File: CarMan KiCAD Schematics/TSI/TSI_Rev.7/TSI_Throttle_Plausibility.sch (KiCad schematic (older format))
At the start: 67 parts, among them Q2 MMBF170, SW1 TS5A3159DBVT, U16 TS372CDT, U18 MCP6004, U23 DAC5574IDGS, U3 TS912, U30 TLP293, U6 TS912, U7 MCP6004, U8 74ACT11030

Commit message: TSI Should be final schematic
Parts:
- removed U18, U7: MCP6004, TSI_Rev_2021_Footprint_Lib:SOIC127P600X175-14N, symbol TSI_Rev.5-rescue:MCP6004-Amplifier_Operational
- added R126: 5.1K, symbol Device:R
- added R127: 10K, symbol Device:R
- added U18, U7: TLV2464CDR, CarMan General Footprints:SOIC127P600X175-14N, symbol CarMan_KiCAD_Library:TLV2464CDR
- C10, C11, C15, C16, C22, C25, C26, C27, C3, C7, C8: footprint Capacitor_SMD:C_0805_2012Metric_Pad1.15x1.40mm_HandSolder -> Capacitor_SMD:C_0805_2012Metric_Pad1.18x1.45mm_HandSolder
- D2: footprint Package_SO:SO-8_5.3x6.2mm_P1.27mm -> Package_SO:MSOP-8_3x3mm_P0.65mm
- R1, R103, R124, R125, R17, R18, R19, R20, R21, R22, R23, R24, R26, R27, R28, R29, R30, R31, R32, R34, R35, R36, R37, R38, R39, R40, R42, R43, R44, R48, R49, R5, R60, R8, R98: footprint Resistor_SMD:R_0805_2012Metric_Pad1.15x1.40mm_HandSolder -> Resistor_SMD:R_0805_2012Metric_Pad1.20x1.40mm_HandSolder
- SW1: footprint TSI_Rev_2021_Footprint_Lib:SOT95P280X145-6N -> SOT95P280X145-6N
- U16: footprint TSI_Rev_2021_Footprint_Lib:SOIC127P600X175-8N -> SOIC127P600X175-8N
- U23: footprint TSI_Rev_2021_Footprint_Lib:DAC5574IDGS -> CarMan General Footprints:SOP50P490X110-10N
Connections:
- net labels added: Throttle_EN
- net labels removed: Throttle_SEL
- wire segments 277 -> 291
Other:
- note added: "A switch that is controlled by\nThrottle_EN. Pin 1 shorted to\npin 4 when pin 6 HIGH"
- note added: "Gain of 1.51 so that max output of DAC (3.3v) translates to 5V\n3.3*1.51=5"
- note added: "PIC SOFTWARE THROTTLE"
- note added: "PIC THROTTLE ENABLE SWITCH"
- note added: "Through ADC to PIC"
- note removed: "A switch that is controlled by\nThrottle_SEL. Pin 1 shorted to\npin 4 when pin 6 HIGH"
- note removed: "AUTO TURN OFF SWITCH"
- moved on the sheet: C16, C22, C25, C26, D11, D4, JP1, Q2, R103, R124, R125, R22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

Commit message: Pre-review_schematic
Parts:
- R126, R127: footprint (none) -> Resistor_SMD:R_0805_2012Metric_Pad1.20x1.40mm_HandSolder
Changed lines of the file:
@@
 F 0 "R126" V 12293 2250 50  0000 C CNN
 F 1 "5.1K" V 12384 2250 50  0000 C CNN
-F 2 "" V 12430 2250 50  0001 C CNN
+F 2 "Resistor_SMD:R_0805_2012Metric_Pad1.20x1.40mm_HandSolder" V 12430 2250 50  0001 C CNN
 F 3 "~" H 12500 2250 50  0001 C CNN
 	1    12500 2250
@@
 F 0 "R127" H 13020 2546 50  0000 L CNN
 F 1 "10K" H 13020 2455 50  0000 L CNN
-F 2 "" V 12880 2500 50  0001 C CNN
+F 2 "Resistor_SMD:R_0805_2012Metric_Pad1.20x1.40mm_HandSolder" V 12880 2500 50  0001 C CNN
 F 3 "~" H 12950 2500 50  0001 C CNN
 	1    12950 2500

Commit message: TSI Post-Nadovich
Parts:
- removed JP1: Jumper_NC_Dual, Connector_PinHeader_2.54mm:PinHeader_1x03_P2.54mm_Vertical, symbol TSI_Rev.5-rescue:Jumper_NC_Dual-Device
- removed R124: 59.7K, Resistor_SMD:R_0805_2012Metric_Pad1.20x1.40mm_HandSolder, symbol TSI_Rev.5-rescue:R-Device
- removed R125: 4.7K, Resistor_SMD:R_0805_2012Metric_Pad1.20x1.40mm_HandSolder, symbol TSI_Rev.5-rescue:R-Device
- removed R126: 5.1K, Resistor_SMD:R_0805_2012Metric_Pad1.20x1.40mm_HandSolder, symbol Device:R
- removed R127: 10K, Resistor_SMD:R_0805_2012Metric_Pad1.20x1.40mm_HandSolder, symbol Device:R
- removed R30: 9.31K, Resistor_SMD:R_0805_2012Metric_Pad1.20x1.40mm_HandSolder, symbol TSI_Rev.5-rescue:R-Device
- removed R31, R60: 499, Resistor_SMD:R_0805_2012Metric_Pad1.20x1.40mm_HandSolder, symbol TSI_Rev.5-rescue:R-Device
- removed R48: 100K, Resistor_SMD:R_0805_2012Metric_Pad1.20x1.40mm_HandSolder, symbol TSI_Rev.5-rescue:R-Device
- removed unit 4 of U18
- removed U23: DAC5574IDGS, CarMan General Footprints:SOP50P490X110-10N, symbol TSI_Rev.5-rescue:DAC5574IDGS-CarMan_KiCAD_Library-TSI_Rev.5-rescue
- added U47: MCP23008-xSS, Package_SO:SSOP-20_5.3x7.2mm_P0.65mm, symbol Interface_Expansion:MCP23008-xSS
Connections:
- net labels added: 0.24V_REF, 4.76V_REF, SCL_5V, SDA_5V
- net labels removed: Throttle_LOGIC
- wire segments 291 -> 284
- no-connect marks 3 -> 4
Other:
- note added: "Brake Light\n(J18)"
- note added: "Brake Pressed Switch\n(J17)"
- note added: "I2C Address 0x20 \n(0100000 - 0100[A2 A1 A0])"
- note added: "Open/Short Window \nRef Voltage Generators"
- note removed: "0.24V"
- note removed: "4.76V"
- note removed: "BRAKE PRESSED"
- note removed: "Brake & BOT\n(J17)"
- note removed: "Brake Light & RTDS\n(J18)"
- note removed: "Gain of 1.51 so that max output of DAC (3.3v) translates to 5V\n3.3*1.51=5"
- note removed: "I2C Address: 0x4D\n(1001101-10011[A1,A0])"
- note removed: "PIC SOFTWARE THROTTLE"
- moved on the sheet: R32, R34, R35, R39, R43

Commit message: TSI REV7 Final Schematic before Layout
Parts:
- removed C25: 0.1u, Capacitor_SMD:C_0805_2012Metric_Pad1.18x1.45mm_HandSolder, symbol TSI_Rev.5-rescue:CAP-pspice
- removed TP18: Pedal Out, TestPoint:TestPoint_Pad_D3.0mm, symbol TSI_Rev.5-rescue:TestPoint-Connector
- added C39: 0.1u, Capacitor_SMD:C_0805_2012Metric_Pad1.18x1.45mm_HandSolder, symbol TSI_Rev.5-rescue:CAP-pspice
- added J28: Pedal_Out TP, symbol Connector_Generic:Conn_01x02
- R49: value 2.4K -> 10K
- R98: value 1K -> 10K
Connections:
- wire segments 284 -> 286
- no-connect marks 4 -> 3
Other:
- moved on the sheet: R44, SW1
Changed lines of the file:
@@
 Wire Wire Line
 	10450 4800 10450 4900
-Text Label 10450 5600 0    50   ~ 0
-5V
-Wire Wire Line
-	10450 5600 10450 5450
-$Comp
-L TSI_Rev.5-rescue:CAP-pspice C25
-U 1 1 6093E057
-P 10450 5200
-F 0 "C25" H 10550 5100 50  0000 C CNN
-F 1 "0.1u" H 10550 5300 50  0000 C CNN
-F 2 "Capacitor_SMD:C_0805_2012Metric_Pad1.18x1.45mm_HandSolder" H 10450 5200 50  0001 C CNN
-F 3 "~" H 10450 5200 50  0001 C CNN
-	1    10450 5200
-	1    0    0    -1
-$EndComp
 Text Label 11350 4250 0    50   ~ 0
 Pedal_Out
@@
 $EndComp
 Connection ~ 5400 4950
-Text Label 15150 4900 2    50   ~ 0
-GLV_RTN
-Text Label 15150 4100 2    50   ~ 0
+Text Label 15500 4450 2    50   ~ 0
+GLV_RTN
+Text Label 15500 3650 2    50   ~ 0
 5V
-Text Label 12725 4500 0    50   ~ 0
+Text Label 13075 4050 0    50   ~ 0
 Throttle_LV
 Text Notes 3050 675  0    79   ~ 0
@@
 P 14200 9000
 F 0 "R49" V 14100 9000 50  0000 C CNN
-F 1 "2.4K" V 14200 9000 50  0000 C CNN
+F 1 "10K" V 14200 9000 50  0000 C CNN
 F 2 "Resistor_SMD:R_0805_2012Metric_Pad1.20x1.40mm_HandSolder" V 14130 9000 50  0001 C CNN
 F 3 "~" H 14200 9000 50  0001 C CNN
@@
 L TSI_Rev.5-rescue:R-Device R44
 U 1 1 608A2A55
-P 13300 4000
-F 0 "R44" H 13350 4000 50  0000 L BNN
-F 1 "10K" V 13300 3995 50  0000 C CNN
-F 2 "Resistor_SMD:R_0805_2012Metric_Pad1.20x1.40mm_HandSolder" V 13230 4000 50  0001 C CNN
-F 3 "~" H 13300 4000 50  0001 C CNN
-	1    13300 4000
+P 13650 3550
+F 0 "R44" H 13700 3550 50  0000 L BNN
+F 1 "10K" V 13650 3545 50  0000 C CNN
+F 2 "Resistor_SMD:R_0805_2012Metric_Pad1.20x1.40mm_HandSolder" V 13580 3550 50  0001 C CNN
+F 3 "~" H 13650 3550 50  0001 C CNN
+	1    13650 3550
 	-1   0    0    1
 $EndComp
-Text Label 13000 3750 0    50   ~ 0
-GLV_RTN
-Text Label 12700 4300 0    50   ~ 0
+Text Label 13350 3300 0    50   ~ 0
+GLV_RTN
+Text Label 13050 3850 0    50   ~ 0
 Throttle_EN
-Text Notes 13050 3450 0    79   ~ 0
+Text Notes 13400 3000 0    79   ~ 0
 PIC THROTTLE ENABLE SWITCH
 Text HLabel 1550 1800 0    50   Input ~ 0
@@
 Wire Wire Line
 	10850 4900 10450 4900
-Connection ~ 10450 4900
-Wire Wire Line
-	10450 4900 10450 4950
 Wire Wire Line
 	10900 4550 11250 4550
 Wire Wire Line
-	13000 3750 13300 3750
-Wire Wire Line
-	13300 3750 13300 3850
-Wire Wire Line
-	14800 4900 15150 4900
-Wire Wire Line
-	14800 4100 15150 4100
+	13350 3300 13650 3300
+Wire Wire Line
+	13650 3300 13650 3400
+Wire Wire Line
+	15150 4450 15500 4450
+Wire Wire Line
+	15150 3650 15500 3650
 Wire Notes Line
 	12800 8900 12800 8650
@@
 Text HLabel 1550 2950 0    50   Output ~ 0
 Brake_Light_RTN
-Text Notes 13525 5350 0    51   ~ 0
+Text Notes 13875 4900 0    51   ~ 0
 A switch that is controlled by\nThrottle_EN. Pin 1 shorted to\npin 4 when pin 6 HIGH
 Wire Wire Line
@@
 P 15050 9500
 F 0 "R98" V 14950 9500 50  0000 C CNN
-F 1 "1K" V 15050 9500 50  0000 C CNN
+F 1 "10K" V 15050 9500 50  0000 C CNN
 F 2 "Resistor_SMD:R_0805_2012Metric_Pad1.20x1.40mm_HandSolder" V 14980 9500 50  0001 C CNN
 F 3 "~" H 15050 9500 50  0001 C CNN
@@
 *0-5V Range*
 Wire Wire Line
-	12725 4500 13400 4500
+	13075 4050 13750 4050
 Text Notes 4300 7750 0    47   ~ 0
 *If the APPS1_ISO and APPS2_b fall \noutside the range of 0.24V-4.76V a \nshort/open is assumed*
@@
 	1    9700 9500
 	0    1    1    0
-$EndComp
-$Comp
-L TSI_Rev.5-rescue:TestPoint-Connector TP18
-U 1 1 6085F531
-P 12100 4250
-F 0 "TP18" H 12050 4450 50  0000 L CNN
-F 1 "Pedal Out" H 12225 4400 50  0001 L CNN
-F 2 "TestPoint:TestPoint_Pad_D3.0mm" H 12300 4250 50  0001 C CNN
-F 3 "~" H 12300 4250 50  0001 C CNN
-	1    12100 4250
-	1    0    0    -1
 $EndComp
 Text Label 10550 10200 2    50   ~ 0
@@
 	5450 3975 5450 4325
 Wire Notes Line
-	12625 5400 15250 5400
-Wire Notes Line
-	15250 5400 15250 3250
-Wire Notes Line
-	15250 3250 12625 3250
-Wire Notes Line
-	12625 3250 12625 5400
+	12975 4950 15600 4950
+Wire Notes Line
+	15600 4950 15600 2800
+Wire Notes Line
+	15600 2800 12975 2800
+Wire Notes Line
+	12975 2800 12975 4950
 $Comp
 L TSI_Rev.5-rescue:TS5A3159DBVT-CarMan_KiCAD_Library SW1
 U 1 1 5FB86D5A
-P 14100 4500
-F 0 "SW1" H 14100 4900 50  0000 C CNN
-F 1 "TS5A3159DBVT" H 14100 3950 50  0000 C CNN
-F 2 "SOT95P280X145-6N" H 14100 4500 50  0001 L BNN
-F 3 "https://www.ti.com/store/ti/en/p/product/?p=TS5A3159DBVT" H 14100 4500 50  0001 L BNN
-F 4 "Analog Switch" H 14100 4500 50  0001 C CNN "Details"
-	1    14100 4500
-	1    0    0    -1
-$EndComp
-Wire Wire Line
-	12700 4300 13300 4300
-Wire Wire Line
-	13300 4150 13300 4300
-Connection ~ 13300 4300
-Wire Wire Line
-	13300 4300 13400 4300
+P 14450 4050
+F 0 "SW1" H 14450 4450 50  0000 C CNN
+F 1 "TS5A3159DBVT" H 14450 3500 50  0000 C CNN
+F 2 "SOT95P280X145-6N" H 14450 4050 50  0001 L BNN
+F 3 "https://www.ti.com/store/ti/en/p/product/?p=TS5A3159DBVT" H 14450 4050 50  0001 L BNN
+F 4 "Analog Switch" H 14450 4050 50  0001 C CNN "Details"
+	1    14450 4050
+	1    0    0    -1
+$EndComp
+Wire Wire Line
+	13050 3850 13650 3850
+Wire Wire Line
+	13650 3700 13650 3850
+Connection ~ 13650 3850
+Wire Wire Line
+	13650 3850 13750 3850
 $Comp
 L TSI_Rev.5-rescue:R-Device R42
@@
 Wire Notes Line
 	8150 9050 11050 9050
-Wire Wire Line
-	12450 4250 12450 4700
-Wire Wire Line
-	12450 4700 13400 4700
-Wire Wire Line
-	11350 4250 12100 4250
-Connection ~ 12100 4250
-Wire Wire Line
-	12100 4250 12450 4250
 Wire Wire Line
 	6450 4650 7250 4650
@@
 Text Label 8750 7325 2    50   ~ 0
 GLV_RTN
-Wire Wire Line
-	8750 5950 8750 5675
 Text Label 8750 5675 2    50   ~ 0
 5V
 NoConn ~ 8250 6250
 NoConn ~ 8250 6150
-NoConn ~ 9250 6150
 NoConn ~ 9250 6550
 Text Notes 9325 7550 2    50   ~ 0
@@
 Wire Notes Line
 	500  500  500  3975
+Text Notes 9500 5600 2    50   ~ 0
+Decoupling Cap\n
+Text Label 9600 5800 0    50   ~ 0
+GLV_RTN
+Wire Wire Line
+	9600 5800 9450 5800
+$Comp
+L TSI_Rev.5-rescue:CAP-pspice C39
+U 1 1 62333FA0
+P 9200 5800
+F 0 "C39" V 9300 5650 50  0000 C CNN
+F 1 "0.1u" V 9300 5950 50  0000 C CNN
+F 2 "Capacitor_SMD:C_0805_2012Metric_Pad1.18x1.45mm_HandSolder" H 9200 5800 50  0001 C CNN
+F 3 "~" H 9200 5800 50  0001 C CNN
+	1    9200 5800
+	0    -1   -1   0
+$EndComp
+Wire Wire Line
+	8750 5675 8750 5800
+Wire Wire Line
+	8750 5800 8950 5800
+Connection ~ 8750 5800
+Wire Wire Line
+	8750 5800 8750 5950
+Wire Wire Line
+	9250 6150 9750 6150
+Text Label 9750 6150 2    39   ~ 0
+5V
+$Comp
+L Connector_Generic:Conn_01x02 J28
+U 1 1 624F25DF
+P 12150 3850
+F 0 "J28" V 12250 3650 50  0000 R CNN
+F 1 "Pedal_Out TP" V 12150 3700 50  0000 R CNN
+F 2 "" H 12150 3850 50  0001 C CNN
+F 3 "~" H 12150 3850 50  0001 C CNN
+	1    12150 3850
+	0    -1   -1   0
+$EndComp
+Wire Wire Line
+	12150 4050 11900 4050
+Wire Wire Line
+	12250 4050 12250 4250
+Text Label 11900 4050 2    39   ~ 0
+GLV_RTN
+Connection ~ 12250 4250
+Wire Wire Line
+	12250 4250 13750 4250
+Wire Wire Line
+	11350 4250 12250 4250
 $EndSCHEMATC

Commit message: Fixed missing footprint on J28
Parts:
- J28: footprint (none) -> Connector_PinSocket_2.54mm:PinSocket_1x02_P2.54mm_Vertical
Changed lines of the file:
@@
 F 0 "J28" V 12250 3650 50  0000 R CNN
 F 1 "Pedal_Out TP" V 12150 3700 50  0000 R CNN
-F 2 "" H 12150 3850 50  0001 C CNN
+F 2 "Connector_PinSocket_2.54mm:PinSocket_1x02_P2.54mm_Vertical" H 12150 3850 50  0001 C CNN
 F 3 "~" H 12150 3850 50  0001 C CNN
 	1    12150 3850

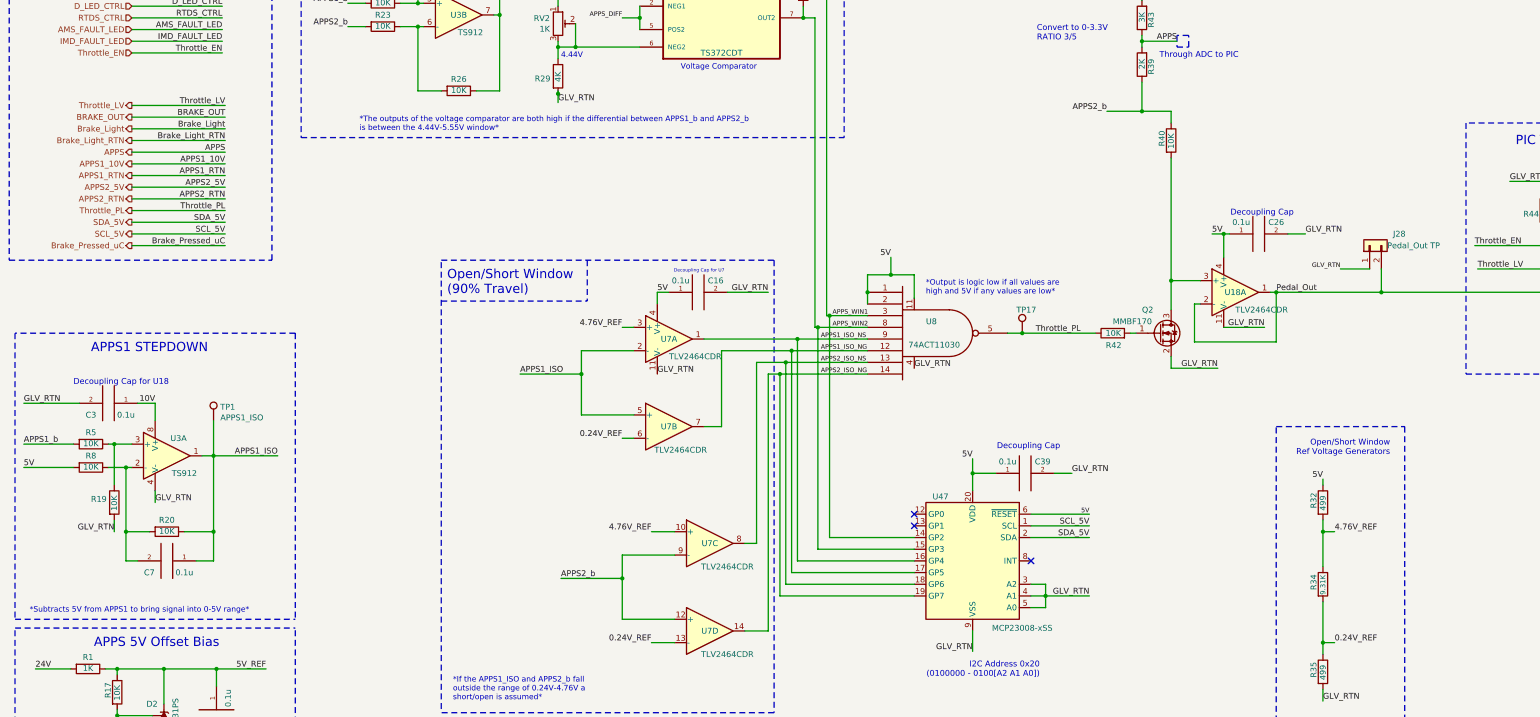
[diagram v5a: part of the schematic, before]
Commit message: Updated Schematic and removed extra footprints from PCB. Ready to begin routing new elements in.
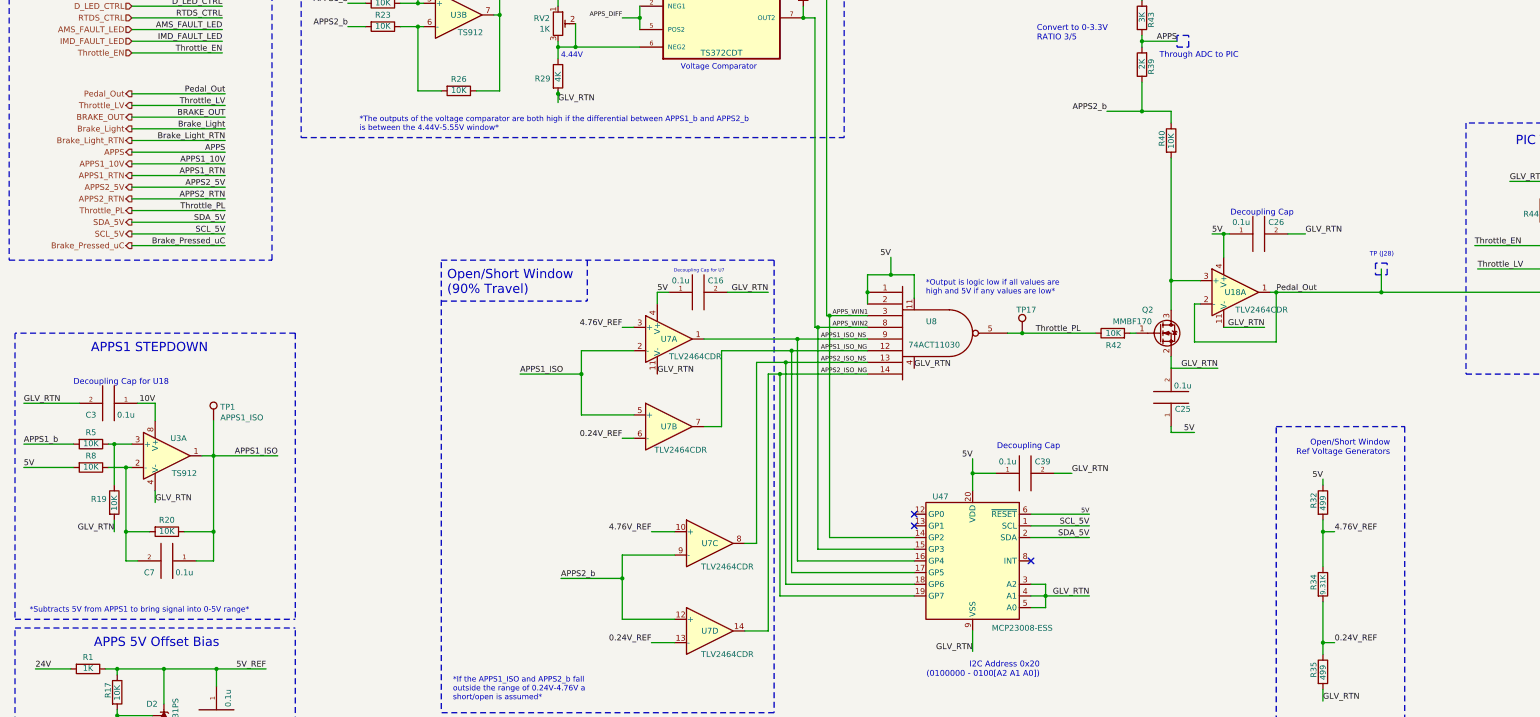
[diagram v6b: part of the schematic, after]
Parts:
- removed J28: Pedal_Out TP, Connector_PinSocket_2.54mm:PinSocket_1x02_P2.54mm_Vertical, symbol Connector_Generic:Conn_01x02
- added C25: 0.1u, Capacitor_SMD:C_0805_2012Metric_Pad1.18x1.45mm_HandSolder, symbol TSI_Rev.5-rescue:CAP-pspice
- U47: value MCP23008-xSS -> MCP23008-ESS
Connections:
- wire segments 286 -> 288
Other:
- note added: "TP (J28)"
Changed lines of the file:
@@
 P 8750 6550
 F 0 "U47" H 9025 7100 50  0000 C CNN
-F 1 "MCP23008-xSS" H 8325 5975 50  0000 C CNN
+F 1 "MCP23008-ESS" H 8325 5975 50  0000 C CNN
 F 2 "Package_SO:SSOP-20_5.3x7.2mm_P0.65mm" H 8750 5500 50  0001 C CNN
 F 3 "http://ww1.microchip.com/downloads/en/DeviceDoc/MCP23008-MCP23S08-Data-Sheet-20001919F.pdf" H 10050 5350 50  0001 C CNN
@@
 Text Label 9750 6150 2    39   ~ 0
 5V
-$Comp
-L Connector_Generic:Conn_01x02 J28
-U 1 1 624F25DF
-P 12150 3850
-F 0 "J28" V 12250 3650 50  0000 R CNN
-F 1 "Pedal_Out TP" V 12150 3700 50  0000 R CNN
-F 2 "Connector_PinSocket_2.54mm:PinSocket_1x02_P2.54mm_Vertical" H 12150 3850 50  0001 C CNN
-F 3 "~" H 12150 3850 50  0001 C CNN
-	1    12150 3850
-	0    -1   -1   0
-$EndComp
-Wire Wire Line
-	12150 4050 11900 4050
 Wire Wire Line
 	12250 4050 12250 4250
-Text Label 11900 4050 2    39   ~ 0
-GLV_RTN
 Connection ~ 12250 4250
 Wire Wire Line
@@
 Wire Wire Line
 	11350 4250 12250 4250
+Text Label 10650 5450 2    50   ~ 0
+5V
+Wire Wire Line
+	10450 5450 10450 5400
+Wire Wire Line
+	10650 5450 10450 5450
+$Comp
+L TSI_Rev.5-rescue:CAP-pspice C25
+U 1 1 6237D884
+P 10450 5150
+F 0 "C25" H 10350 5250 50  0000 C CNN
+F 1 "0.1u" H 10350 5050 50  0000 C CNN
+F 2 "Capacitor_SMD:C_0805_2012Metric_Pad1.18x1.45mm_HandSolder" H 10450 5150 50  0001 C CNN
+F 3 "~" H 10450 5150 50  0001 C CNN
+	1    10450 5150
+	-1   0    0    1
+$EndComp
+Wire Notes Line
+	12200 4000 12200 4100
+Wire Notes Line
+	12200 4100 12300 4100
+Wire Notes Line
+	12300 4100 12300 4000
+Wire Notes Line
+	12300 4000 12200 4000
+Text Notes 12150 3950 0    39   ~ 0
+TP (J28)
+Wire Wire Line
+	2350 2550 1550 2550
+Text HLabel 1550 2550 0    50   Output ~ 0
+Pedal_Out
+Text Label 2350 2550 2    50   ~ 0
+Pedal_Out
 $EndSCHEMATC
